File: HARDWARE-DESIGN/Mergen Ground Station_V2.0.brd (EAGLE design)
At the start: 72.4 x 94.9 mm, 68 parts, among them J1 USB_A_SMT_FEMALE_NS, J2 CON-SD-CARD_MICROSD-2908-05, J4 U.FL, U1 STM32F302C8T6, U13 L86, U15 AMS1117-5V, U16 AMS1117-3.3, X2 JST-XH-04-PIN-LONG-PAD, Y1 ABMM2-8.000MHZ-E2-T

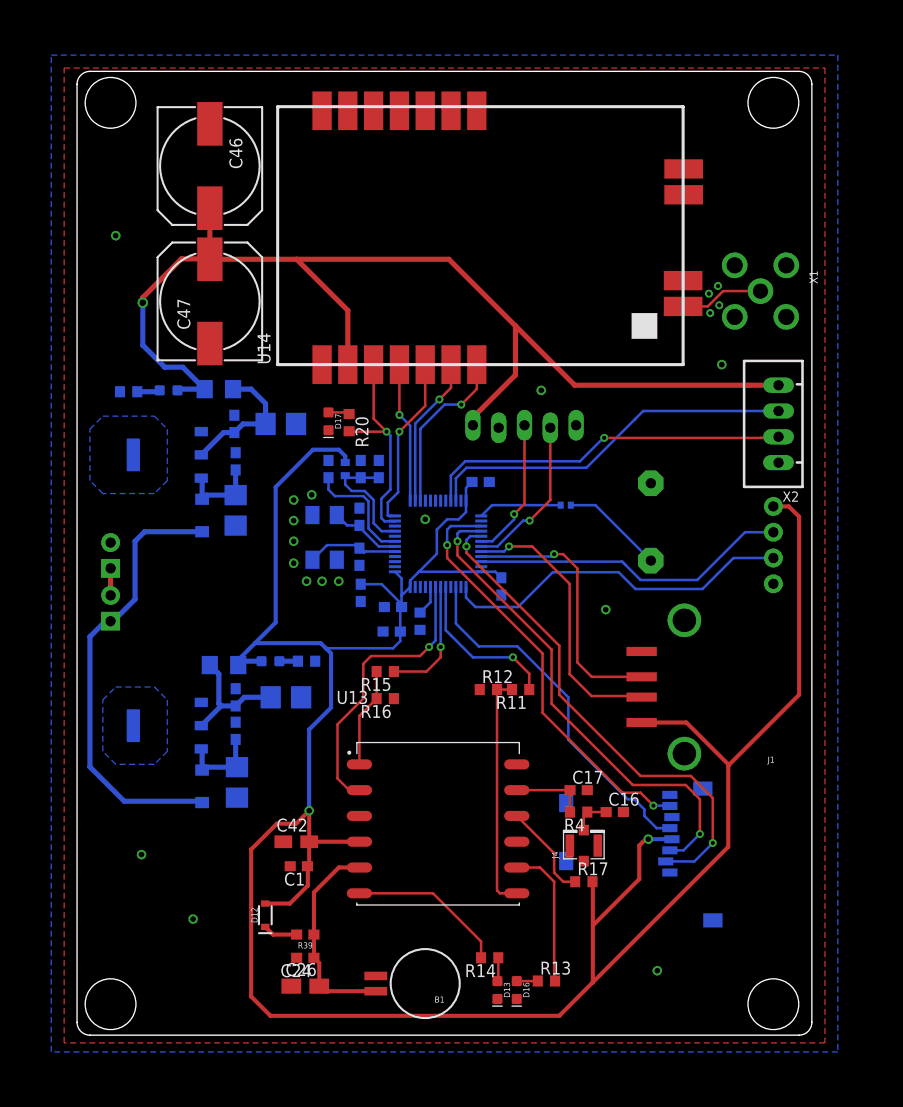
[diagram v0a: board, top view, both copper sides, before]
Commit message: Polygon 15 mils
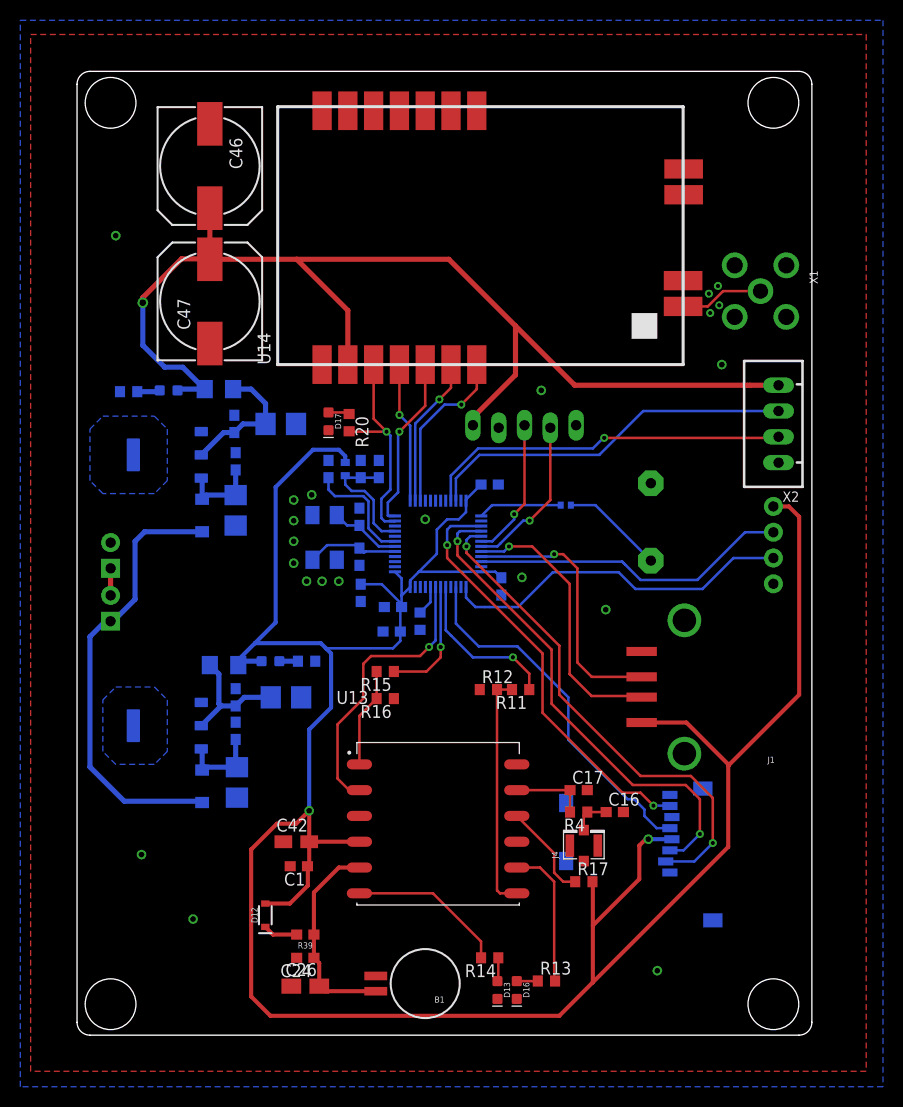
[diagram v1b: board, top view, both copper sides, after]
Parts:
- moved C19 0.92 mm to (40.6, 59.3)
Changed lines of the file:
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@@
 <setting verticaltext="up"/>
 </settings>
-<grid distance="50" unitdist="mil" unit="mil" style="lines" multiple="1" display="no" altdistance="5" altunitdist="mil" altunit="mil"/>
+<grid distance="5" unitdist="mil" unit="mil" style="lines" multiple="1" display="no" altdistance="5" altunitdist="mil" altunit="mil"/>
 <layers>
 <layer number="1" name="Top" color="4" fill="1" visible="yes" active="yes"/>
@@
 <attribute name="VALUE" x="31.75" y="45.339" size="1.27" layer="28" rot="MR0"/>
 </element>
-<element name="C19" library="rcl" library_urn="urn:adsk.eagle:library:334" package="C0603" package3d_urn="urn:adsk.eagle:package:23616/2" value="100nF" x="39.751" y="59.563" smashed="yes" rot="MR180">
-<attribute name="NAME" x="39.116" y="58.928" size="1.27" layer="26" rot="MR180"/>
-<attribute name="POPULARITY" value="73" x="121.031" y="143.383" size="1.778" layer="28" rot="MR180" display="off"/>
-<attribute name="SPICEPREFIX" value="C" x="121.031" y="143.383" size="1.778" layer="28" rot="MR180" display="off"/>
-<attribute name="VALUE" x="39.116" y="61.468" size="1.27" layer="28" rot="MR180"/>
+<element name="C19" library="rcl" library_urn="urn:adsk.eagle:library:334" package="C0603" package3d_urn="urn:adsk.eagle:package:23616/2" value="100nF" x="40.64" y="59.309" smashed="yes" rot="MR180">
+<attribute name="NAME" x="40.005" y="58.674" size="1.27" layer="26" rot="MR180"/>
+<attribute name="POPULARITY" value="73" x="121.92" y="143.129" size="1.778" layer="28" rot="MR180" display="off"/>
+<attribute name="SPICEPREFIX" value="C" x="121.92" y="143.129" size="1.778" layer="28" rot="MR180" display="off"/>
+<attribute name="VALUE" x="40.005" y="61.214" size="1.27" layer="28" rot="MR180"/>
 </element>
 <element name="C2" library="rcl" library_urn="urn:adsk.eagle:library:334" package="CT3528" package3d_urn="urn:adsk.eagle:package:23325/2" value="22uF" x="15.621" y="56.769" smashed="yes" rot="MR270">
@@
 <contactref element="Y1" pad="2"/>
 <contactref element="Y1" pad="4"/>
-<polygon width="0.3048" layer="1" rank="2">
-<vertex x="-1.27" y="100.33"/>
-<vertex x="73.66" y="100.33"/>
-<vertex x="73.66" y="4.318"/>
-<vertex x="-1.27" y="4.318"/>
+<polygon width="0.381" layer="1" rank="2">
+<vertex x="-4.572" y="103.632"/>
+<vertex x="77.724" y="103.632"/>
+<vertex x="77.724" y="1.524"/>
+<vertex x="-4.572" y="1.524"/>
 </polygon>
-<polygon width="0.3048" layer="16" rank="2">
-<vertex x="-2.54" y="101.6"/>
-<vertex x="74.93" y="101.6"/>
-<vertex x="74.93" y="3.429"/>
-<vertex x="-2.54" y="3.429"/>
+<polygon width="0.381" layer="16" rank="2">
+<vertex x="-5.588" y="105.029"/>
+<vertex x="79.375" y="105.029"/>
+<vertex x="79.375" y="0"/>
+<vertex x="-5.588" y="0"/>
 </polygon>
 <contactref element="U1" pad="47"/>
@@
 <contactref element="U1" pad="35"/>
 <contactref element="U1" pad="8"/>
-<polygon width="0.3048" layer="16">
+<polygon width="0.381" layer="16">
 <vertex x="2.54" y="33.02"/>
 <vertex x="2.54" y="38.1"/>
@@
 <vertex x="3.81" y="31.75"/>
 </polygon>
-<polygon width="0.3048" layer="16">
+<polygon width="0.381" layer="16">
 <vertex x="1.27" y="59.69"/>
 <vertex x="1.27" y="64.77"/>
@@
 <contactref element="X2" pad="1"/>
 <via x="34.29" y="55.88" extent="1-16" drill="0.55"/>
+<via x="43.815" y="50.165" extent="1-16" drill="0.55"/>
 </signal>
 <signal name="FN">
@@
 <wire x1="27.94" y1="49.491" x2="30.011" y2="49.491" width="0.254" layer="16"/>
 <wire x1="31.965" y1="47.537" x2="30.011" y2="49.491" width="0.254" layer="16"/>
-<wire x1="38.31" y1="58.972" x2="38.901" y2="59.563" width="0.254" layer="16"/>
+<wire x1="38.31" y1="57.829" x2="39.79" y2="59.309" width="0.254" layer="16"/>
 <wire x1="22.86" y1="27.178" x2="21.59" y2="25.908" width="0.4064" layer="1"/>
 <wire x1="47.498" y1="6.985" x2="50.8" y2="10.287" width="0.4064" layer="1"/>
@@
 <wire x1="39.81" y1="50.717" x2="41.192" y2="50.717" width="0.254" layer="16"/>
 <wire x1="41.192" y1="50.717" x2="41.783" y2="50.126" width="0.254" layer="16"/>
-<wire x1="38.31" y1="57.717" x2="38.31" y2="58.972" width="0.254" layer="16"/>
+<wire x1="38.31" y1="57.717" x2="38.31" y2="57.829" width="0.254" layer="16"/>
 <wire x1="31.965" y1="47.244" x2="31.965" y2="48.372" width="0.254" layer="16"/>
 <wire x1="31.965" y1="48.372" x2="32.81" y2="49.217" width="0.254" layer="16"/>
@@
 </signal>
 <signal name="TX3">
-<wire x1="36.81" y1="60.178" x2="38.227" y2="61.595" width="0.254" layer="16"/>
-<wire x1="38.227" y1="61.595" x2="49.53" y2="61.595" width="0.254" layer="16"/>
+<wire x1="36.81" y1="60.178" x2="39.497" y2="62.865" width="0.254" layer="16"/>
+<wire x1="39.497" y1="62.865" x2="50.8" y2="62.865" width="0.254" layer="16"/>
 <wire x1="51.92250625" y1="63.90149375" x2="51.83649375" y2="63.90149375" width="0.254" layer="16"/>
-<wire x1="51.83649375" y1="63.90149375" x2="49.53" y2="61.595" width="0.254" layer="16"/>
+<wire x1="51.83649375" y1="63.90149375" x2="50.8" y2="62.865" width="0.254" layer="16"/>
 <via x="51.92250625" y="63.90149375" extent="1-16" drill="0.4"/>
-<wire x1="51.92250625" y1="63.90149375" x2="67.31" y2="63.90149375" width="0.254" layer="1"/>
+<wire x1="51.92250625" y1="63.90149375" x2="68.98149375" y2="63.90149375" width="0.254" layer="1"/>
 <contactref element="U1" pad="21"/>
-<wire x1="67.31" y1="63.90149375" x2="67.47450625" y2="63.90149375" width="0.254" layer="1"/>
 <wire x1="36.81" y1="57.717" x2="36.81" y2="60.178" width="0.254" layer="16"/>
 <contactref element="X2" pad="2"/>
-<wire x1="67.47450625" y1="63.90149375" x2="68.98149375" y2="63.90149375" width="0.254" layer="1"/>
 <wire x1="68.98149375" y1="63.90149375" x2="69.088" y2="64.008" width="0.254" layer="1"/>
 </signal>
 <signal name="RX3">
-<wire x1="37.31" y1="59.916" x2="38.354" y2="60.96" width="0.254" layer="16"/>
-<wire x1="38.354" y1="60.96" x2="50.165" y2="60.96" width="0.254" layer="16"/>
-<wire x1="50.165" y1="60.96" x2="54.9275" y2="65.7225" width="0.254" layer="16"/>
+<wire x1="37.31" y1="59.916" x2="39.624" y2="62.23" width="0.254" layer="16"/>
+<wire x1="39.624" y1="62.23" x2="51.435" y2="62.23" width="0.254" layer="16"/>
+<wire x1="51.435" y1="62.23" x2="55.753" y2="66.548" width="0.254" layer="16"/>
 <contactref element="U1" pad="22"/>
-<wire x1="54.9275" y1="65.7225" x2="54.975" y2="65.77" width="0.254" layer="16"/>
 <wire x1="37.31" y1="57.717" x2="37.31" y2="59.916" width="0.254" layer="16"/>
 <contactref element="X2" pad="3"/>
-<wire x1="54.975" y1="65.77" x2="55.753" y2="66.548" width="0.254" layer="16"/>
 <wire x1="55.753" y1="66.548" x2="69.088" y2="66.548" width="0.254" layer="16"/>
 </signal>

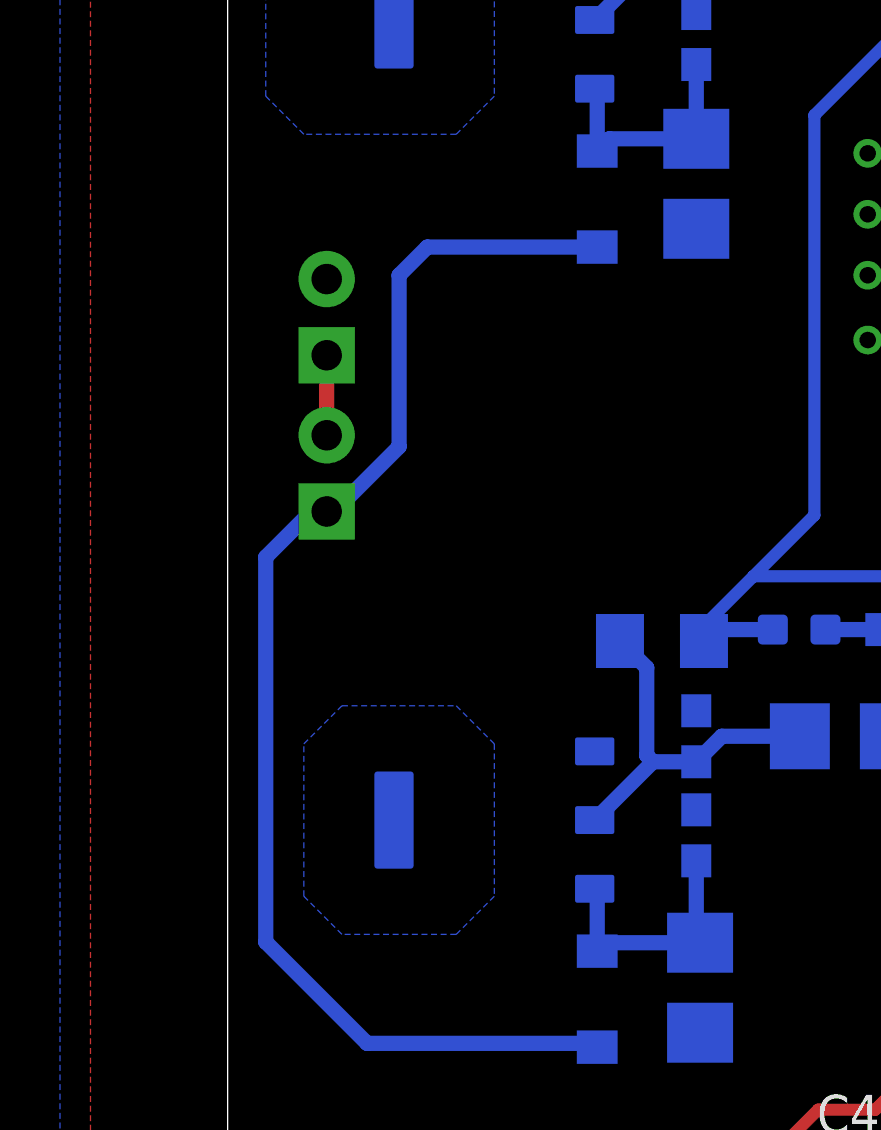
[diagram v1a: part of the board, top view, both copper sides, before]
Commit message: Terminal Blocks were changed
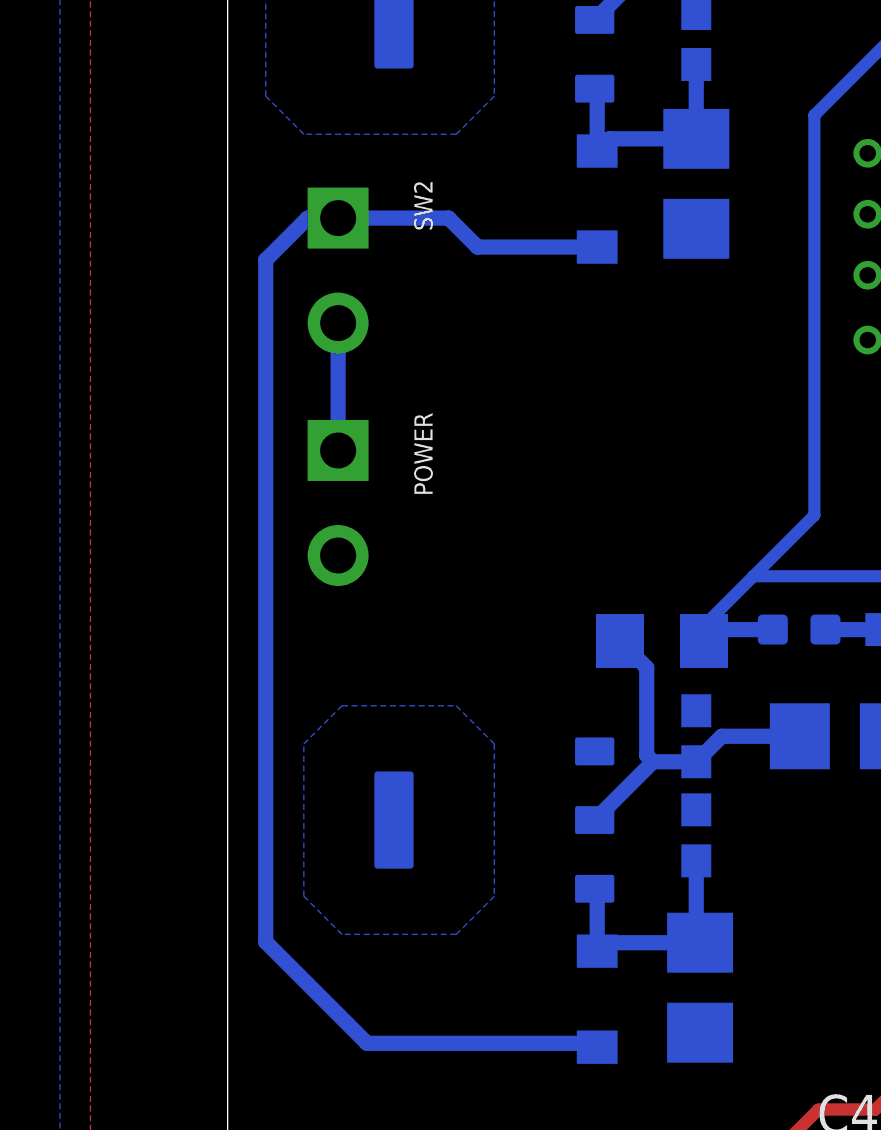
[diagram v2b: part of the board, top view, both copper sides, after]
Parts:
- removed BT1, SW1: (no value), SparkFun-Connectors:MOLEX-1X2
- added POWER, SW2: (no value), SparkFun-Connectors:SCREWTERMINAL-3.5MM-2-NS
- D10, D11: value MBR0520LT1G -> B5819W
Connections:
- net GND: now also POWER.2; no longer BT1.2
- net N$30: now also POWER.1, SW2.2; no longer BT1.1, SW1.2
- net VCC: now also SW2.1; no longer SW1.1
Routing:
- net VCC: track 44.0 -> 47.3 mm
- net N$30: track 2.67 -> 4.25 mm
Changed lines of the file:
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@@
 <attribute name="VALUE" x="36.195" y="10.16" size="0.6096" layer="27" font="vector" ratio="20" rot="R180"/>
-</element>
-<element name="BT1" library="SparkFun-Connectors" library_urn="urn:adsk.eagle:library:513" package="MOLEX-1X2" package3d_urn="urn:adsk.eagle:package:38040/1" value="" x="3.302" y="51.054" smashed="yes" rot="MR90">
-<attribute name="NAME" x="6.604" y="49.784" size="0.6096" layer="26" font="vector" ratio="20" rot="MR90"/>
-<attribute name="SF_ID" value="PRT-09918" x="-72.898" y="77.724" size="1.778" layer="28" rot="MR90" display="off"/>
-<attribute name="VALUE" x="0.508" y="49.784" size="0.6096" layer="28" font="vector" ratio="20" rot="MR90" align="top-left"/>
 </element>
 <element name="C1" library="rcl" library_urn="urn:adsk.eagle:library:334" package="C0603" package3d_urn="urn:adsk.eagle:package:23616/2" value="100nF" x="21.844" y="21.717" smashed="yes" rot="R180">
@@
 <attribute name="VALUE" x="13.716" y="34.417" size="1.27" layer="28" rot="MR90"/>
 </element>
-<element name="D10" library="Diode" library_urn="urn:adsk.eagle:library:16378169" package="SODFL3718X115" package3d_urn="urn:adsk.eagle:package:9427153/2" value="MBR0520LT1G" x="12.319" y="56.261" smashed="yes" rot="MR270">
+<element name="D10" library="Diode" library_urn="urn:adsk.eagle:library:16378169" package="SODFL3718X115" package3d_urn="urn:adsk.eagle:package:9427153/2" value="B5819W" x="12.319" y="56.261" smashed="yes" rot="MR270">
 <attribute name="CATEGORY" value="Diode" x="88.519" y="9.271" size="1.778" layer="28" rot="MR270" display="off"/>
 <attribute name="DESCRIPTION" value="DIODE SCHOTTKY 20V 500MA SOD123" x="88.519" y="9.271" size="1.778" layer="28" rot="MR270" display="off"/>
@@
 <attribute name="ZENER_VOLTAGE" value="" x="88.519" y="9.271" size="1.778" layer="28" rot="MR270" display="off"/>
 </element>
-<element name="D11" library="Diode" library_urn="urn:adsk.eagle:library:16378169" package="SODFL3718X115" package3d_urn="urn:adsk.eagle:package:9427153/2" value="MBR0520LT1G" x="12.319" y="29.591" smashed="yes" rot="MR270">
+<element name="D11" library="Diode" library_urn="urn:adsk.eagle:library:16378169" package="SODFL3718X115" package3d_urn="urn:adsk.eagle:package:9427153/2" value="B5819W" x="12.319" y="29.591" smashed="yes" rot="MR270">
 <attribute name="CATEGORY" value="Diode" x="88.519" y="-31.369" size="1.778" layer="28" rot="MR270" display="off"/>
 <attribute name="DESCRIPTION" value="DIODE SCHOTTKY 20V 500MA SOD123" x="88.519" y="-31.369" size="1.778" layer="28" rot="MR270" display="off"/>
@@
 <attribute name="VALUE" x="66.548" y="48.26" size="0.6096" layer="28" font="vector" ratio="20" rot="MR90"/>
 </element>
-<element name="SW1" library="SparkFun-Connectors" library_urn="urn:adsk.eagle:library:513" package="MOLEX-1X2" package3d_urn="urn:adsk.eagle:package:38040/1" value="" x="3.302" y="45.847" smashed="yes" rot="MR90">
-<attribute name="NAME" x="6.604" y="44.577" size="0.6096" layer="26" font="vector" ratio="20" rot="MR90"/>
-<attribute name="SF_ID" value="PRT-09918" x="-72.898" y="78.867" size="1.778" layer="28" rot="MR90" display="off"/>
-<attribute name="VALUE" x="0.508" y="44.577" size="0.6096" layer="28" font="vector" ratio="20" rot="MR90" align="top-left"/>
-</element>
 <element name="U13" library="L86" package="XCVR_L86" value="L86" x="35.56" y="25.4" smashed="yes">
 <attribute name="AVAILABILITY" value="Unavailable" x="90.17" y="12.7" size="1.778" layer="27" display="off"/>
@@
 <attribute name="VALUE" x="65.1955" y="59.2755" size="1.016" layer="27" ratio="10" rot="R90"/>
 </element>
+<element name="POWER" library="SparkFun-Connectors" library_urn="urn:adsk.eagle:library:513" package="SCREWTERMINAL-3.5MM-2-NS" package3d_urn="urn:adsk.eagle:package:38055/1" value="" x="3.683" y="47.879" smashed="yes" rot="R270">
+<attribute name="NAME" x="6.223" y="49.149" size="0.6096" layer="25" font="vector" ratio="20" rot="R270"/>
+<attribute name="PROD_ID" value="CONN-08399" x="3.683" y="47.879" size="1.778" layer="27" rot="R270" display="off"/>
+<attribute name="VALUE" x="4.953" y="49.149" size="0.6096" layer="27" font="vector" ratio="20" rot="R270"/>
+</element>
+<element name="SW2" library="SparkFun-Connectors" library_urn="urn:adsk.eagle:library:513" package="SCREWTERMINAL-3.5MM-2-NS" package3d_urn="urn:adsk.eagle:package:38055/1" value="" x="3.683" y="55.626" smashed="yes" rot="R270">
+<attribute name="NAME" x="6.223" y="56.896" size="0.6096" layer="25" font="vector" ratio="20" rot="R270"/>
+<attribute name="PROD_ID" value="CONN-08399" x="3.683" y="55.626" size="1.778" layer="27" rot="R270" display="off"/>
+<attribute name="VALUE" x="4.953" y="56.896" size="0.6096" layer="27" font="vector" ratio="20" rot="R270"/>
+</element>
 </elements>
 <signals>
@@
 <contactref element="D10" pad="2"/>
 <contactref element="D11" pad="2"/>
-<contactref element="SW1" pad="1"/>
-<wire x1="3.302" y1="45.847" x2="2.794" y2="45.847" width="0.508" layer="16"/>
-<wire x1="2.794" y1="45.847" x2="1.27" y2="44.323" width="0.508" layer="16"/>
-<wire x1="1.27" y1="44.323" x2="1.27" y2="31.496" width="0.508" layer="16"/>
 <wire x1="12.319" y1="27.9906" x2="12.192" y2="28.1176" width="0.508" layer="16"/>
 <wire x1="12.192" y1="28.1176" x2="4.6484" y2="28.1176" width="0.508" layer="16"/>
 <wire x1="4.6484" y1="28.1176" x2="1.27" y2="31.496" width="0.508" layer="16"/>
-<wire x1="3.302" y1="45.847" x2="3.556" y2="45.847" width="0.508" layer="16"/>
-<wire x1="3.556" y1="45.847" x2="5.715" y2="48.006" width="0.508" layer="16"/>
-<wire x1="5.715" y1="48.006" x2="5.715" y2="53.721" width="0.508" layer="16"/>
-<wire x1="6.6546" y1="54.6606" x2="12.319" y2="54.6606" width="0.508" layer="16"/>
-<wire x1="5.715" y1="53.721" x2="6.6546" y2="54.6606" width="0.508" layer="16"/>
+<contactref element="SW2" pad="1"/>
+<wire x1="1.27" y1="54.229" x2="2.667" y2="55.626" width="0.508" layer="16"/>
+<wire x1="2.667" y1="55.626" x2="3.683" y2="55.626" width="0.508" layer="16"/>
+<wire x1="1.27" y1="31.496" x2="1.27" y2="54.229" width="0.508" layer="16"/>
+<wire x1="3.683" y1="55.626" x2="7.366" y2="55.626" width="0.508" layer="16"/>
+<wire x1="8.3314" y1="54.6606" x2="12.319" y2="54.6606" width="0.508" layer="16"/>
+<wire x1="7.366" y1="55.626" x2="8.3314" y2="54.6606" width="0.508" layer="16"/>
 </signal>
 <signal name="GND">
@@
 <contactref element="U14" pad="GND@1"/>
 <contactref element="R12" pad="1"/>
-<contactref element="BT1" pad="2"/>
 <contactref element="STM1" pad="1"/>
 <contactref element="X1" pad="GND4"/>
@@
 <via x="34.29" y="55.88" extent="1-16" drill="0.55"/>
 <via x="43.815" y="50.165" extent="1-16" drill="0.55"/>
+<contactref element="POWER" pad="2"/>
 </signal>
 <signal name="FN">
@@
 </signal>
 <signal name="N$30">
-<contactref element="BT1" pad="1"/>
-<contactref element="SW1" pad="2"/>
-<wire x1="3.302" y1="48.387" x2="3.302" y2="51.054" width="0.508" layer="1"/>
+<contactref element="POWER" pad="1"/>
+<contactref element="SW2" pad="2"/>
+<wire x1="3.683" y1="52.126" x2="3.683" y2="47.879" width="0.508" layer="16"/>
 </signal>
 <signal name="N$31">
